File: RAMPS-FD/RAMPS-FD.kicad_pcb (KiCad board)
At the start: 2 copper layers, 100 x 100 mm, 209 parts, among them J10 1x4PinHeader, J11 1x4PinHeader, J12 1x4PinHeader, J13 2x1PinHeader, J14 1x4PinHeader, J15 1x4PinHeader, J16 1x4PinHeader, J17 1x3PinHeader, J18 2x5PinHeader, J19 1x4PinHeader, J2 2x1PinHeader, J20 1x3PinHeader, J21 2x6PinHeader, J22 1x4PinHeader, J23 3x4PinHeader, J24 1x18PinHeader, J25 2_PinScrewTerminal_P350, J26 2_PinScrewTerminal_P508, J27 2_PinScrewTerminal_P350, J28 2_PinScrewTerminal_P350, J29 3x6PinHeader, J3 6_PinScrewPlugableTerminal_P5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, J30 2x1PinHeader, J31 2x1PinHeader, J32 2x4PinHeader_2.54mm, J5 1x3JumperArray, J6 2x1PinHeader, J7 1x3JumperArray, J8 1x3PinHeader, J9 1x4PinHeader, M2 LOGO_OSHW, Q10 NCE3416, Q11 NCE3416, Q2 NCE3416, Q3 TDM3415, Q4 TDM3415, Q5 NCE3416, Q6 PSMN7R5-60YLX, Q7 PSMN1R8-40YLC, Q8 PSMN7R5-60YLX, Q9 PSMN7R5-60YLX, SW2 PushButton, U10 24C512, U11 MC74LCX07, U2 AS7812ADTR, U3 Pololu, U4 Pololu, U5 Pololu, U6 SN74LV1T125, U7 Pololu, U8 Pololu, U9 Pololu

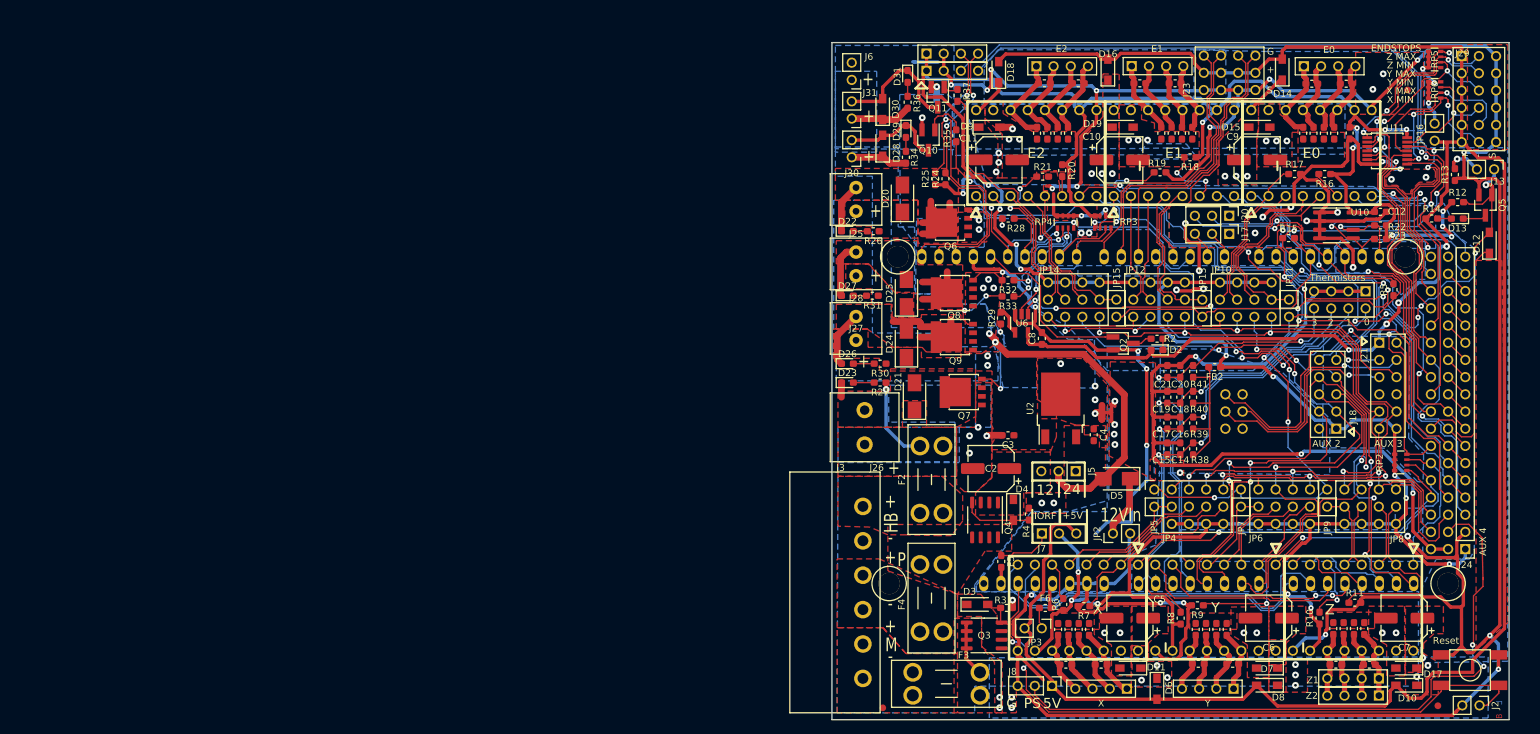
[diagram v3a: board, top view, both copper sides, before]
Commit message: V3 Added, UART support for steppers and improved parts/layout
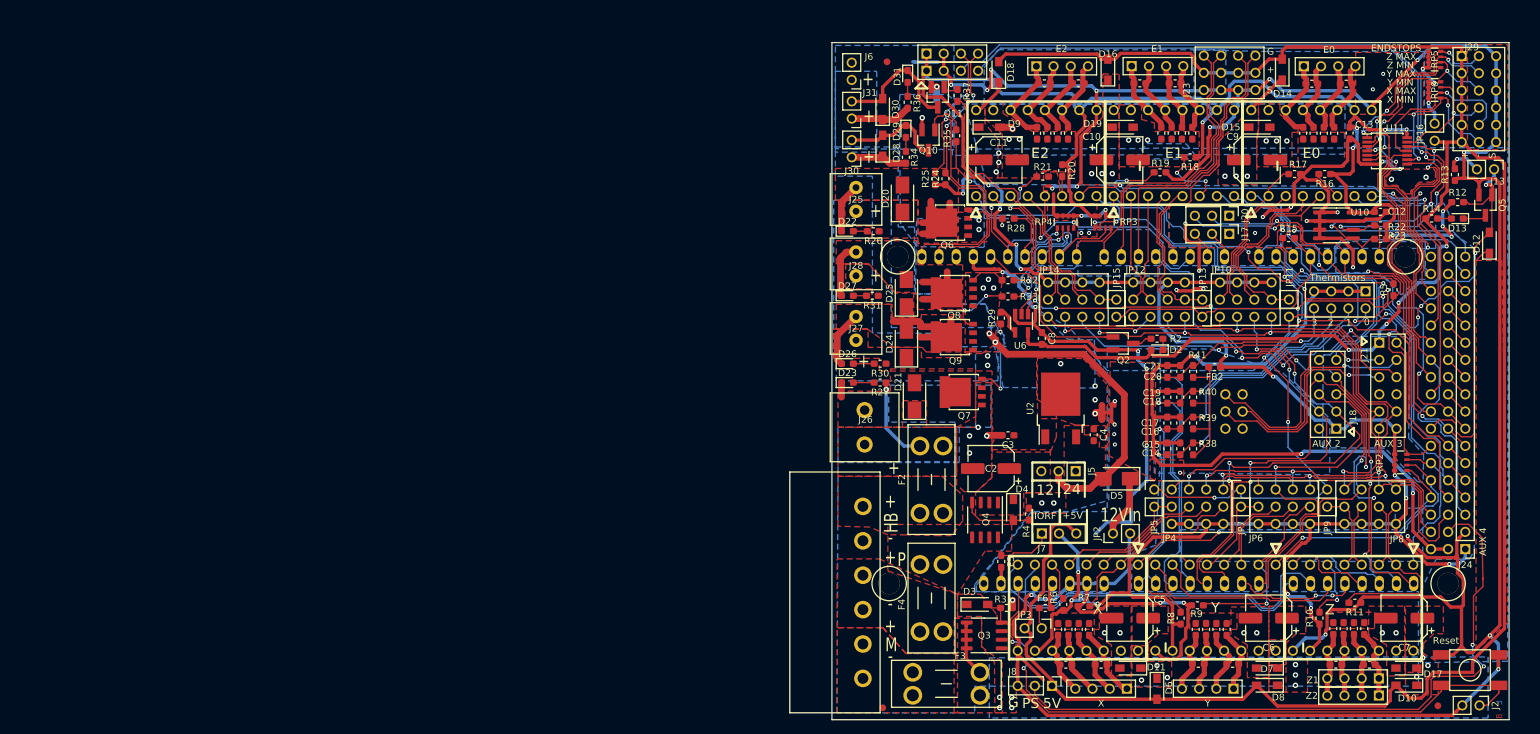
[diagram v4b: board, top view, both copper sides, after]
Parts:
- moved FID3 77.0 mm to (60.5, 42.4)
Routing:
- net Net-(J29-Pad8): track 28.4 -> 29.5 mm
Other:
- net class Default: via_dia 0.8 -> 0.6
- net class high-power: via_dia 1 -> 0.8
- net class low-power: via_dia 0.8 -> 0.6
- net class med-power: via_dia 1 -> 0.8
- net class motor-power: via_dia 1.6256 -> 0.8; via_drill 1.016 -> 0.4
- net class power: via_dia 0.762 -> 0.6; via_drill 0.381 -> 0.3
- board text added: "JLCJLCJLCJLC"
